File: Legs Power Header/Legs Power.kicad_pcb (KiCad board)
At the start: 2 copper layers, 25 parts, among them J10 Conn_01x04_Pin, J11 Conn_01x04_Pin, J12 Conn_01x04_Pin, J13 Conn_01x04_Pin, J14 Conn_01x04_Pin, J15 Conn_01x04_Pin, J16 Conn_01x04_Pin, J17 Conn_01x04_Pin, J18 Conn_01x04_Pin, J19 Conn_01x04_Pin, J2 Conn_01x04_Pin, J20 Conn_01x04_Pin, J21 Conn_01x04_Pin, J22 Conn_01x04_Pin, J23 Conn_01x04_Pin, J24 Conn_01x04_Pin, J25 Conn_01x04_Pin, J26 Conn_01x04_Pin, J3 Conn_01x04_Pin, J4 Conn_01x04_Pin, J5 Conn_01x04_Pin, J7 Conn_01x04_Pin, J8 Conn_01x04_Pin, J9 Conn_01x04_Pin

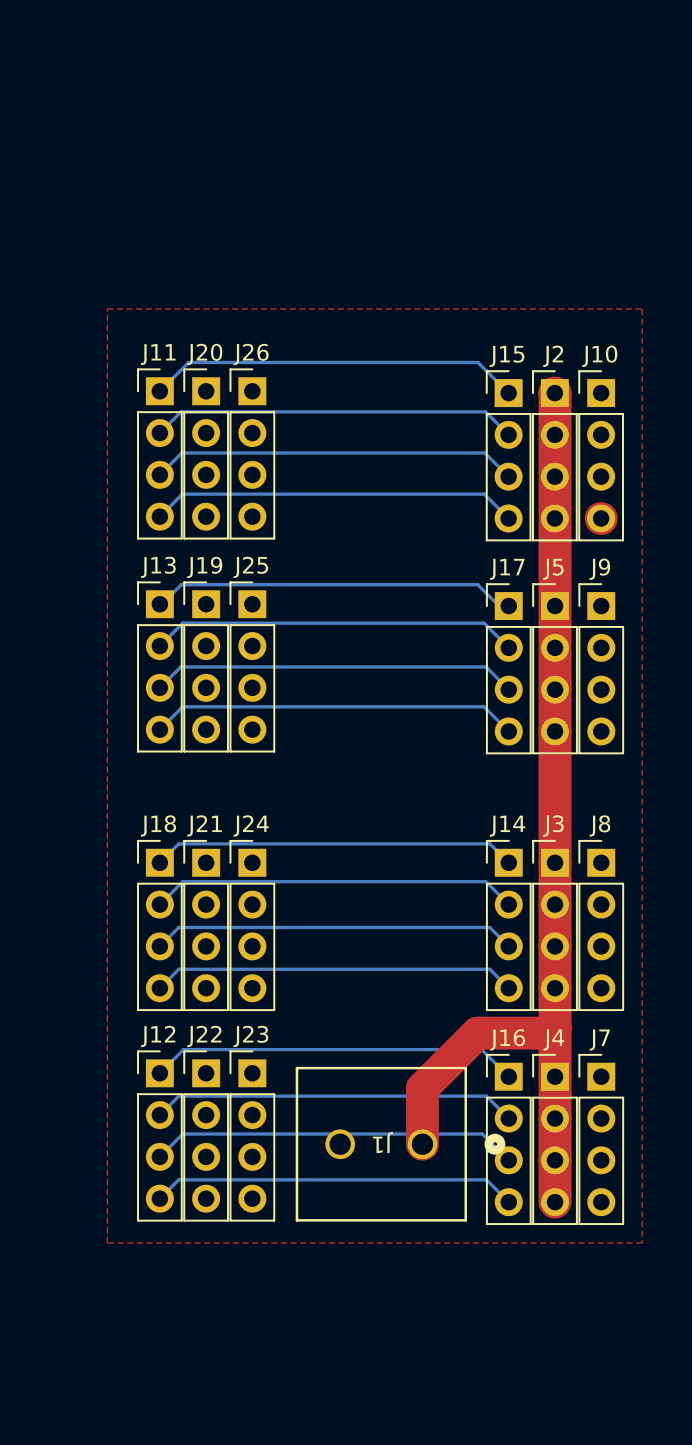
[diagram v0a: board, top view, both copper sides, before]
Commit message: Completed Basic Header Board for Power With Power Supply
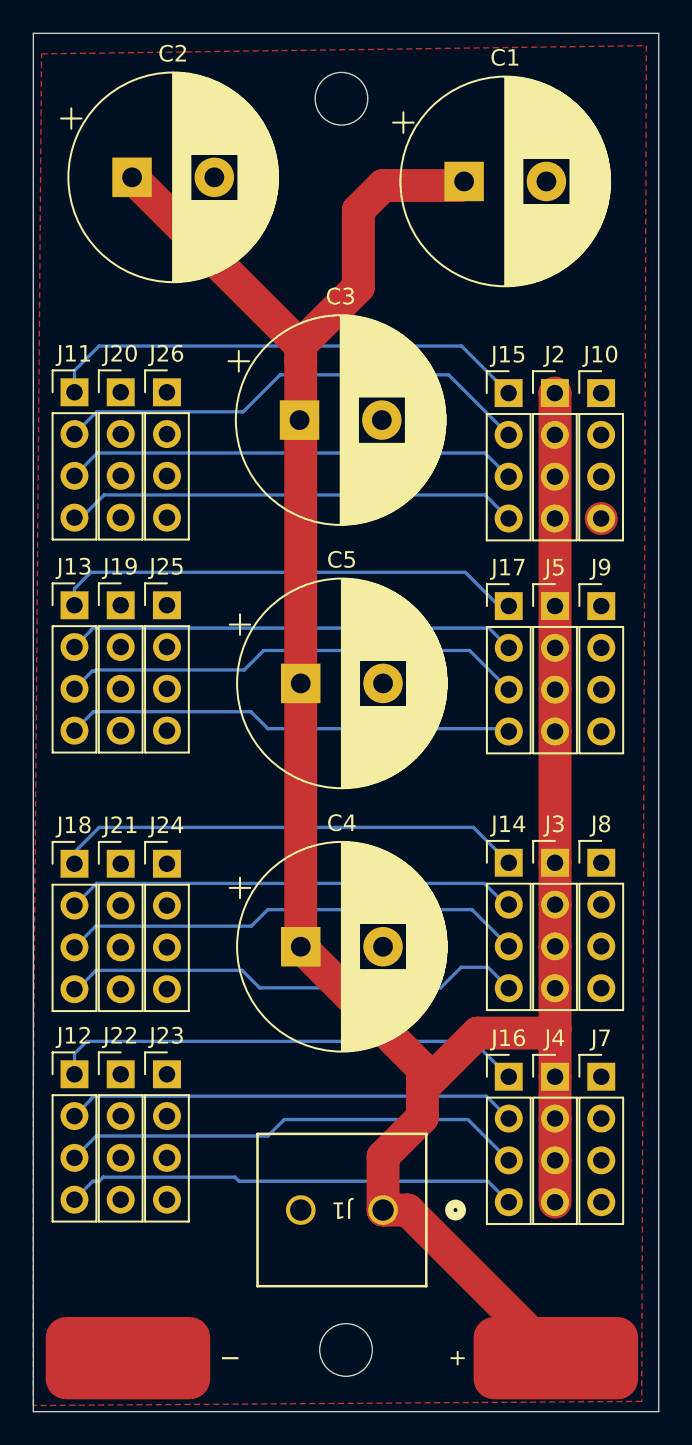
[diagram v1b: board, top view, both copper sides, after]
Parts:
- added +: Batt_POS, Connector_Wire:SolderWirePad_1x01_SMD_5x10mm, F.Cu at (135.2, 104.0)
- added C1: C_Polarized, Capacitor_THT:CP_Radial_D12.5mm_P5.00mm, F.Cu at (129.7, 32.5)
- added C2: C_Polarized, Capacitor_THT:CP_Radial_D12.5mm_P5.00mm, F.Cu at (109.5, 32.2)
- added C3: C_Polarized, Capacitor_THT:CP_Radial_D12.5mm_P5.00mm, F.Cu at (119.7, 47.0)
- added C4: C_Polarized, Capacitor_THT:CP_Radial_D12.5mm_P5.00mm, F.Cu at (119.8, 79.0)
- added C5: C_Polarized, Capacitor_THT:CP_Radial_D12.5mm_P5.00mm, F.Cu at (119.8, 63.0)
- added H1: MountingHole, MountingHole:MountingHole_3.2mm_M3, F.Cu at (122.2, 27.5)
- added H2: MountingHole, MountingHole:MountingHole_3.2mm_M3, F.Cu at (122.5, 103.5)
- added I: I, Connector_Wire:SolderWirePad_1x01_SMD_5x10mm, F.Cu at (109.2, 104.0)
- moved J11 5.19 mm to (106.0, 45.3)
- moved J12 5.19 mm to (106.0, 86.8)
- moved J13 5.19 mm to (106.0, 58.2)
- moved J18 5.19 mm to (106.0, 74.0)
- moved J19 5.19 mm to (108.8, 58.2)
- moved J20 5.19 mm to (108.8, 45.3)
- moved J21 5.19 mm to (108.8, 74.0)
- moved J22 5.19 mm to (108.8, 86.8)
- moved J23 5.19 mm to (111.6, 86.8)
- moved J24 5.19 mm to (111.6, 74.0)
- moved J25 5.19 mm to (111.6, 58.2)
- moved J26 5.19 mm to (111.6, 45.3)
- moved J1 4.66 mm to (124.8, 95.0)
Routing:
- net Net-(J2-Pin_1): track 72.3 -> 170.4 mm
- net Net-(J11-Pin_2): track 22.3 -> 29.4 mm
- net Net-(J11-Pin_1): track 22.7 -> 29.5 mm
- net Net-(J14-Pin_1): track 22.2 -> 28.6 mm
- net Net-(J13-Pin_1): track 22.2 -> 28.7 mm
- net Net-(J12-Pin_1): track 22.5 -> 28.8 mm
- net Net-(J14-Pin_4): track 22.2 -> 28.4 mm
- net Net-(J14-Pin_3): track 22.2 -> 28.3 mm
- net Net-(J13-Pin_3): track 22.3 -> 28.3 mm
- net Net-(J12-Pin_3): track 22.4 -> 28.4 mm
- net Net-(J12-Pin_4): track 22.2 -> 27.6 mm
- net Net-(J12-Pin_2): track 22.2 -> 27.5 mm
- net Net-(J11-Pin_3): track 22.3 -> 27.6 mm
- net Net-(J11-Pin_4): track 22.4 -> 27.5 mm
- net Net-(J14-Pin_2): track 22.4 -> 27.5 mm
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- added copper zone on F.Cu, net Net-(J10-Pin_1)
- removed copper zone on F.Cu, net unconnected-(J19-Pin_2-Pad2)
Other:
- board outline added: 38 x 83.8 mm
